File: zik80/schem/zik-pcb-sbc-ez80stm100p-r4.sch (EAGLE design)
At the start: 107 parts, among them IC1 7432N, IC2 7404N

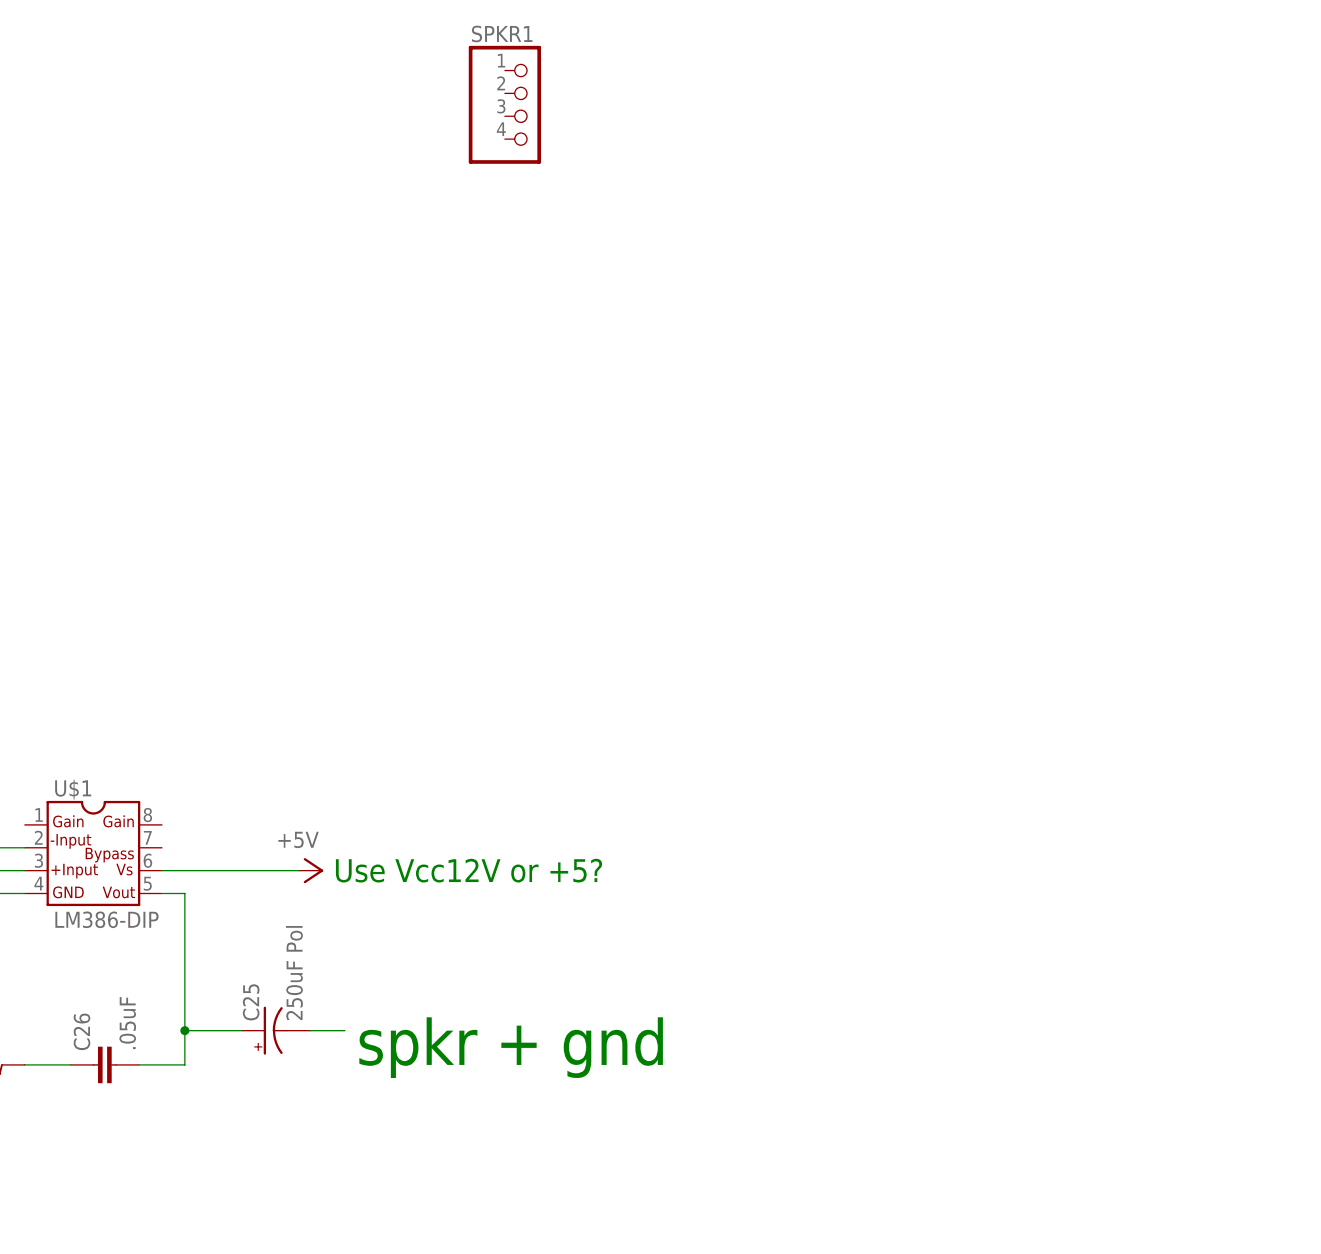
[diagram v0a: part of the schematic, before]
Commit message: adding a audio circuit schem image
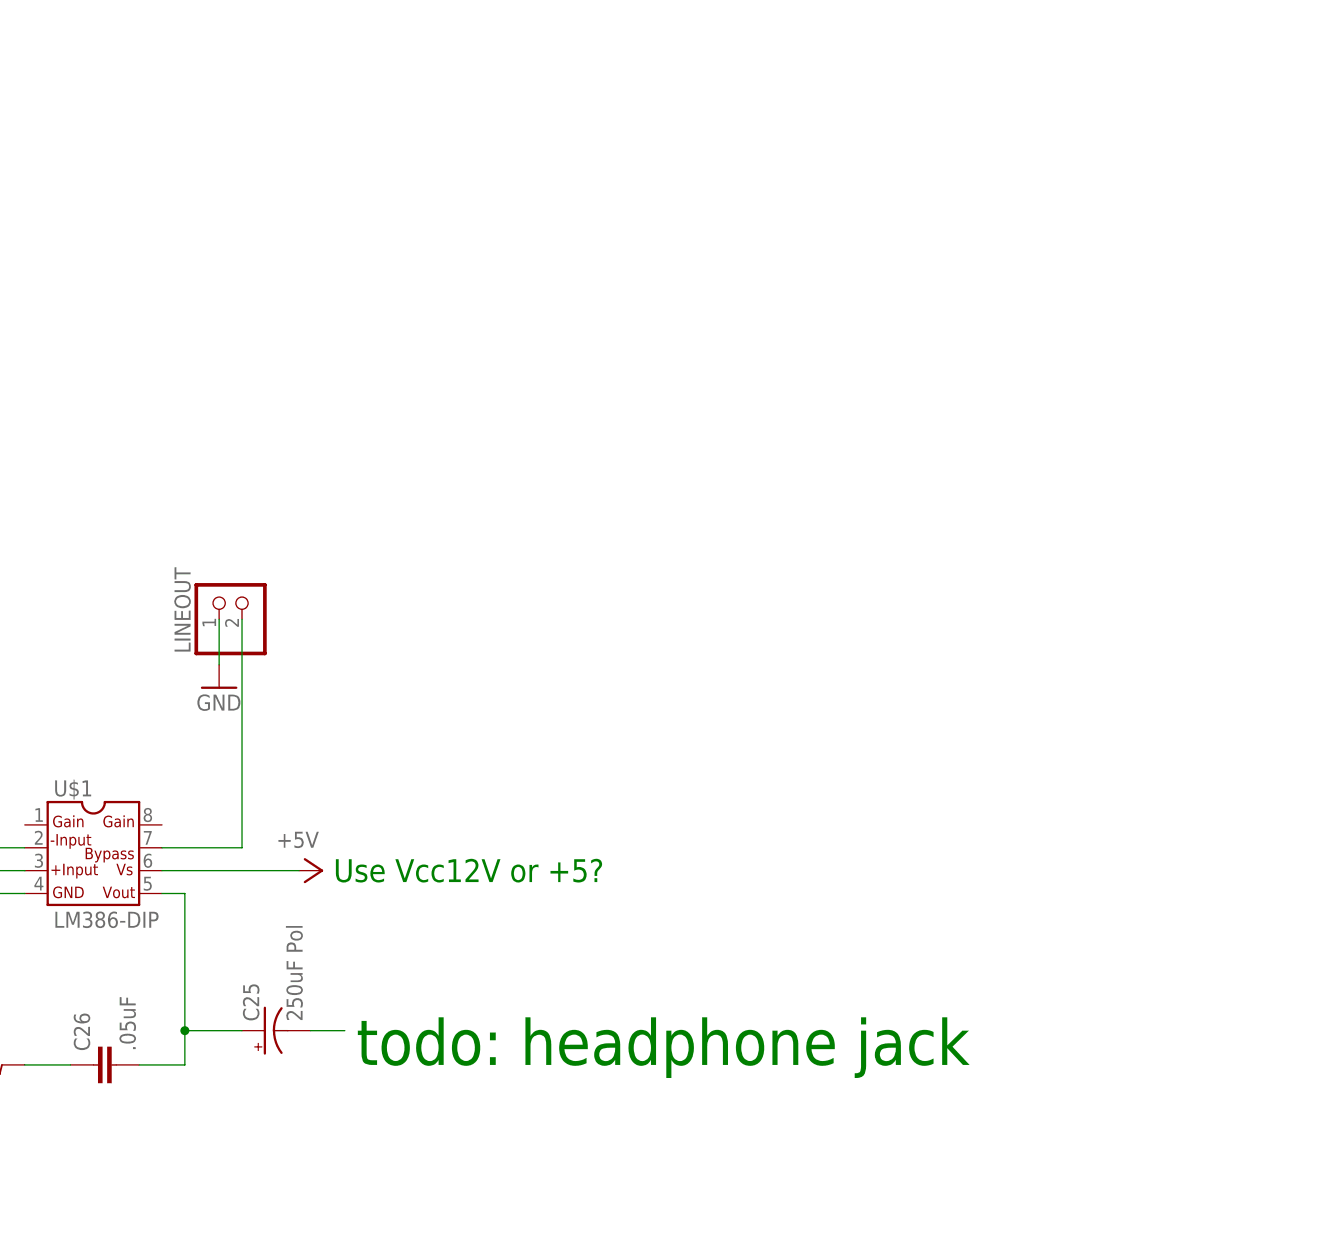
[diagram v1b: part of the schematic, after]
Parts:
- removed SPKR1: (no value), pinhead:PINHD-1X4
- added LINEOUT: (no value), pinhead:PINHD-1X2
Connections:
- new net N$3: LINEOUT.2, U$1.7
- net GND: now also LINEOUT.1
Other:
- note added: "todo: headphone jack"
- note removed: "spkr + gnd"
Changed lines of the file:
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@@
 <part name="3V" library="wirepad" deviceset="WIREPAD" device="SMD1,27-254"/>
 <part name="+3V3" library="supply1" deviceset="+3V3" device=""/>
-<part name="SPKR1" library="pinhead" deviceset="PINHD-1X4" device=""/>
 <part name="R34" library="rcl" deviceset="R-US_" device="0204/7" value="1K"/>
 <part name="C23" library="rcl" deviceset="C-EU" device="025-025X050" value="100uF"/>
@@
 <part name="R37" library="rcl" deviceset="R-US_" device="0204/7" value="10"/>
 <part name="GND41" library="supply1" deviceset="GND" device=""/>
+<part name="LINEOUT" library="pinhead" deviceset="PINHD-1X2" device=""/>
+<part name="GND42" library="supply1" deviceset="GND" device=""/>
 </parts>
 <sheets>
@@
 pins</text>
 <text x="513.08" y="347.98" size="2.54" layer="91">Use Vcc12V or +5?</text>
-<text x="515.62" y="327.66" size="5.08" layer="91">spkr + gnd</text>
+<text x="515.62" y="327.66" size="5.08" layer="91">todo: headphone jack</text>
 <text x="457.2" y="408.94" size="3.81" layer="108">TODO:
 - correct package for
@@
 <instance part="3V" gate="G$1" x="191.77" y="142.24"/>
 <instance part="+3V3" gate="G$1" x="207.01" y="142.24" rot="R270"/>
-<instance part="SPKR1" gate="A" x="534.67" y="433.07"/>
 <instance part="R34" gate="G$1" x="427.99" y="330.2" rot="R270"/>
 <instance part="C23" gate="G$1" x="438.15" y="340.36" rot="R90"/>
@@
 <instance part="R37" gate="G$1" x="473.71" y="327.66"/>
 <instance part="GND41" gate="1" x="463.55" y="327.66" rot="R270"/>
+<instance part="LINEOUT" gate="G$1" x="502.92" y="379.73" rot="R90"/>
+<instance part="GND42" gate="1" x="500.38" y="369.57"/>
 </instances>
 <busses>
@@
 <pinref part="GND41" gate="1" pin="GND"/>
 </segment>
+<segment>
+<pinref part="GND42" gate="1" pin="GND"/>
+<pinref part="LINEOUT" gate="G$1" pin="1"/>
+<wire x1="500.38" y1="372.11" x2="500.38" y2="377.19" width="0.1524" layer="91"/>
+</segment>
 </net>
 <net name="PB6" class="0">
@@
 </segment>
 </net>
+<net name="N$3" class="0">
+<segment>
+<pinref part="U$1" gate="G$1" pin="7"/>
+<wire x1="494.03" y1="351.79" x2="502.92" y2="351.79" width="0.1524" layer="91"/>
+<wire x1="502.92" y1="351.79" x2="502.92" y2="377.19" width="0.1524" layer="91"/>
+<pinref part="LINEOUT" gate="G$1" pin="2"/>
+</segment>
+</net>

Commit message: Added basic -shield schem, as I work on the library parts creation
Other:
- note added: "Use Vcc12V or +5? Decouple Vcc/GND with a cap?"
- note added: "rev 4: Goal: move to sockets on pcb instead of millions of header pins - add mixer hw to audio - add amplifier hw to audio - ?? add SD on pcb? - ?? add USB for direct power? - ?? USB -> ez80? or stm32f4? - ?? newer stm32f5? rev 3: - rotated 180deg ISPZDI - rotated 180deg ISP GPU - Z GPIO-B -> audio data bus now - bump to 512KB SRAM chip, compatible to 256KB and 128KB with fiddling (code level to 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"
- note removed: "Use Vcc12V or +5?"
- note removed: "rev 4: Goal: move to sockets on pcb instead of millions of header pins - add mixer hw to audio - add amplifier hw to audio rev 3: - rotated 180deg ISPZDI - rotated 180deg ISP GPU - Z GPIO-B -> audio data bus now - bump to 512KB SRAM chip, compatible to 256KB and 128KB with fiddling (code level to ensure chip select) - added smd solder pads for PB14/15 - added solder pad for shorting to force RAM 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"
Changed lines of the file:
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@@
 <setting verticaltext="up"/>
 </settings>
-<grid distance="0.05" unitdist="inch" unit="inch" style="dots" multiple="1" display="yes" altdistance="0.01" altunitdist="inch" altunit="inch"/>
+<grid distance="0.1" unitdist="inch" unit="inch" style="lines" multiple="1" display="no" altdistance="0.01" altunitdist="inch" altunit="inch"/>
 <layers>
 <layer number="1" name="Top" color="4" fill="1" visible="no" active="no"/>
@@
 <text x="447.04" y="50.8" size="6.4516" layer="91">Zikzak SBC - Single board computer
 Jeff Mitchell 2014</text>
-<text x="445.77" y="-109.22" size="5.08" layer="91">rev 4:
+<text x="445.77" y="-134.62" size="5.08" layer="91">rev 4:
 Goal: move to sockets on pcb
 instead of millions of header pins
 - add mixer hw to audio
 - add amplifier hw to audio
+- ?? add SD on pcb?
+- ?? add USB for direct power?
+- ?? USB -&gt; ez80? or stm32f4?
+- ?? newer stm32f5?
 rev 3:
 - rotated 180deg ISPZDI
@@
 as needed to feed other
 pins</text>
-<text x="513.08" y="347.98" size="2.54" layer="91">Use Vcc12V or +5?</text>
+<text x="513.08" y="347.98" size="2.54" layer="91">Use Vcc12V or +5?
+Decouple Vcc/GND with a cap?</text>
 <text x="515.62" y="327.66" size="5.08" layer="91">todo: headphone jack</text>
 <text x="457.2" y="408.94" size="3.81" layer="108">TODO:
